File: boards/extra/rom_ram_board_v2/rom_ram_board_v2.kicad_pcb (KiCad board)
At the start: 2 copper layers, 95.2 x 95.2 mm, 24 parts, among them J1 Exp. Conn. A, J2 Exp. Conn. B, J3 Power, J4 Exp. Conn. C, J5 BANK SELECT, U1 74LS139, U2 SST39SF040, U3 AS6C4008-55PCN, U4 AS6C4008-55PCN, U5 AS6C4008-55PCN

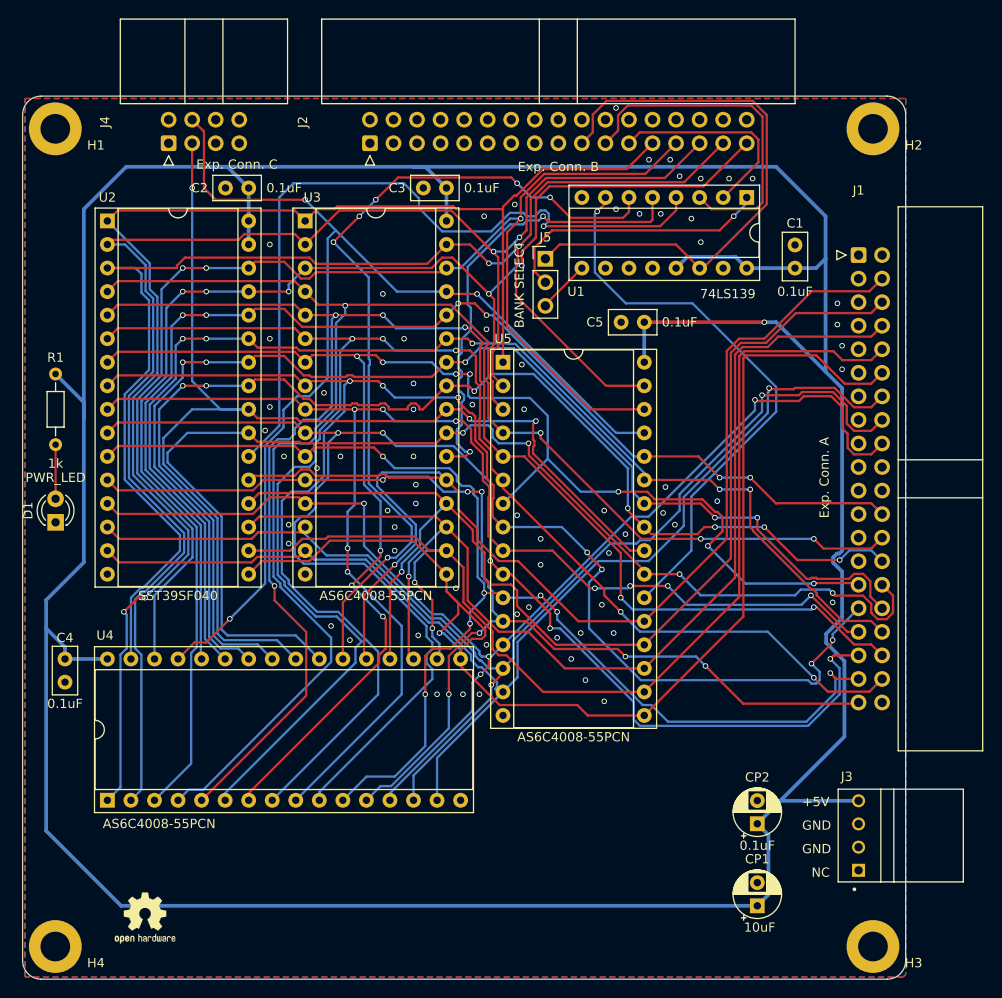
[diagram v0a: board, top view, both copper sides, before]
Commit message: Updated ROM/RAM Board V2
Updated the ROM/RAM Board V2 to revision 1.1
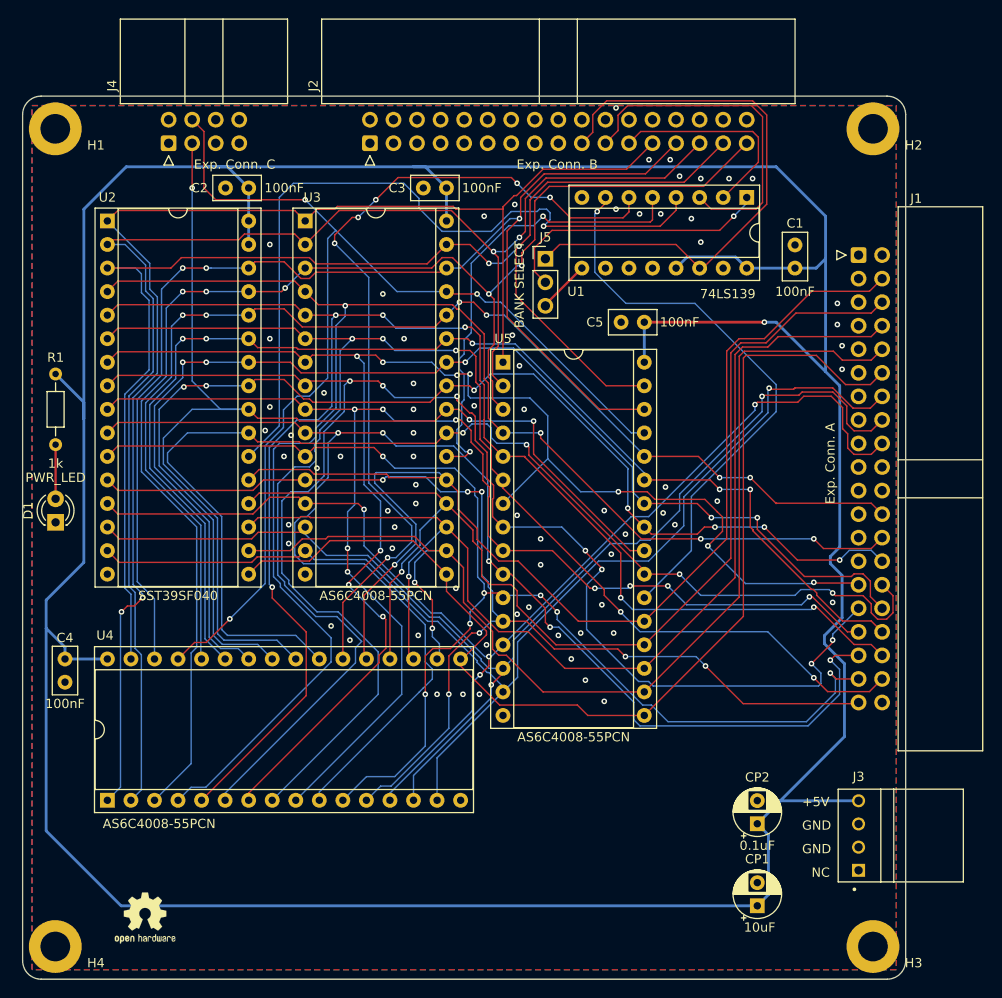
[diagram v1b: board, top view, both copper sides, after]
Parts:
- C1, C2, C3, C4, C5: value 0.1uF -> 100nF
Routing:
- net /B_D3: track 129.4 -> 119.2 mm, vias 1 -> 0
- net /M_A15: track 151.7 -> 147.0 mm
- net /M_A16: track 160.2 -> 155.7 mm
- net /M_A18: track 152.7 -> 148.4 mm
- net /M_A17: track 140.8 -> 136.6 mm
- net /B_A11: track 130.8 -> 128.8 mm
- net /B_A9: track 132.1 -> 130.7 mm
- net /B_A4: track 173.6 -> 174.8 mm
- net /B_D0: track 132.4 -> 131.4 mm
- net /~{MEM_CS2}: track 50.3 -> 49.4 mm
- net /B_A5: track 166.0 -> 166.6 mm
- net /B_A2: track 166.4 -> 165.8 mm
- net /~{MEMR}: track 129.4 -> 128.9 mm
- net /B_D7: track 136.5 -> 137.0 mm
- net /GND: vias 70 -> 72
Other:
- rule pad_to_mask_clearance: 0.2 -> 0
